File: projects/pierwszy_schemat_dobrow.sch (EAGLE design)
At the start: 30 parts, among them IC1 74HC595N, IC2 7805T, U1 ARDUINOR3-BPLACE

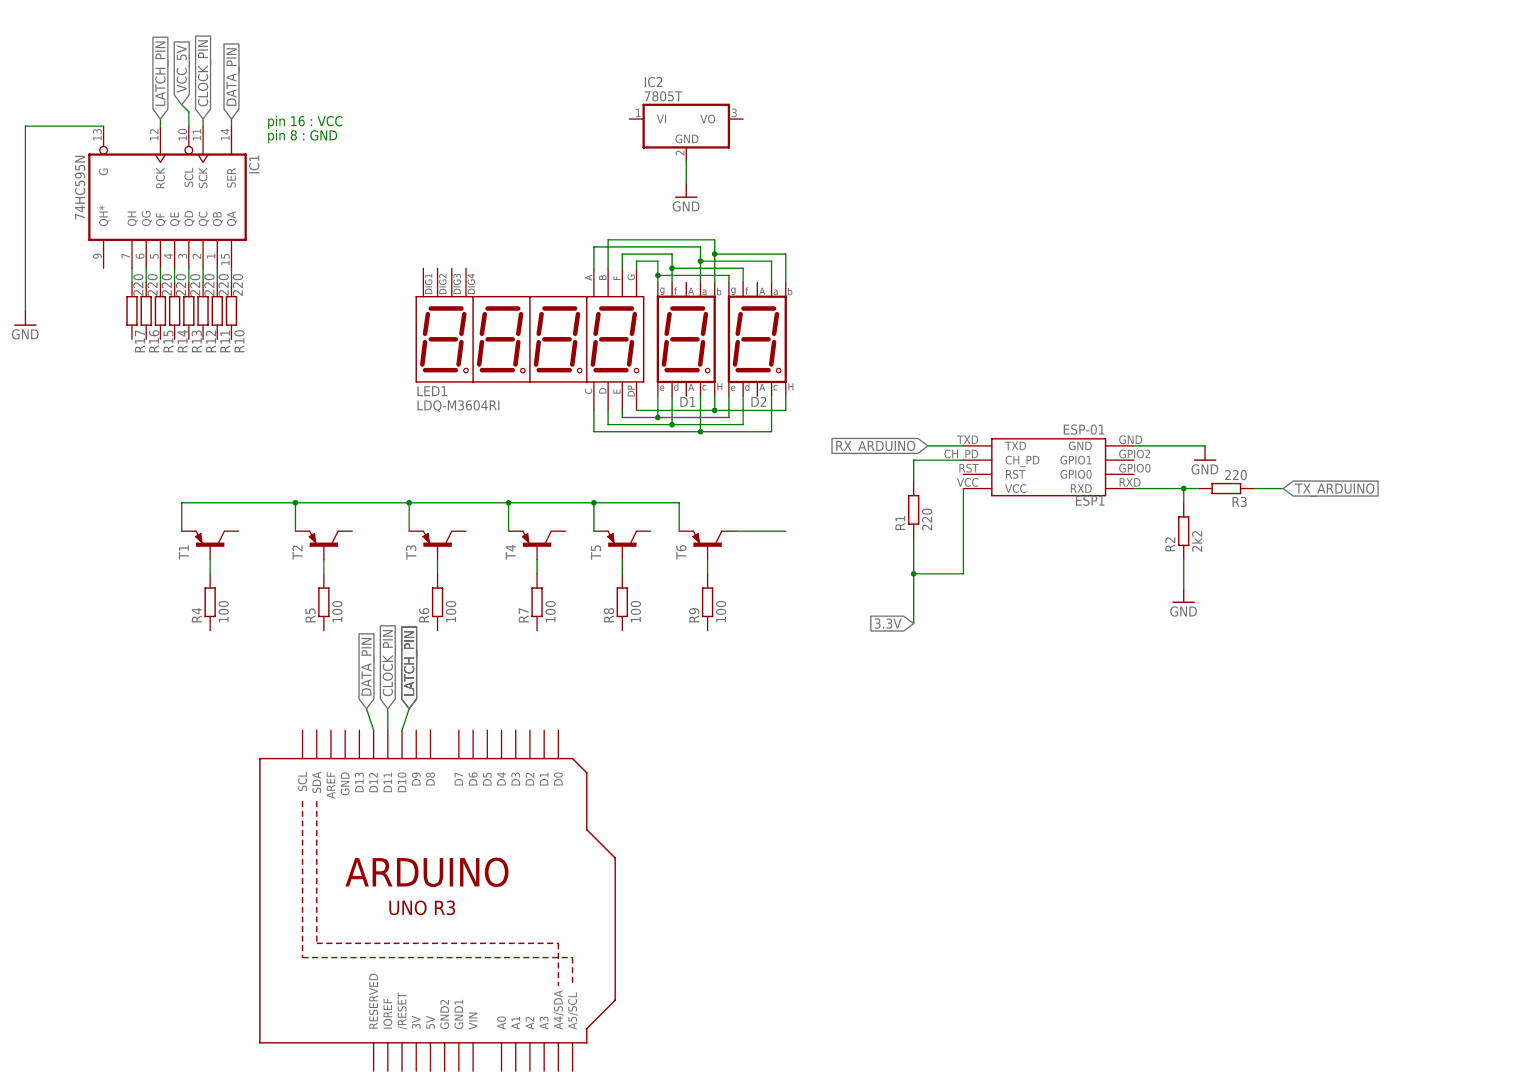
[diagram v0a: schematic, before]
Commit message: new arduino uno symbol
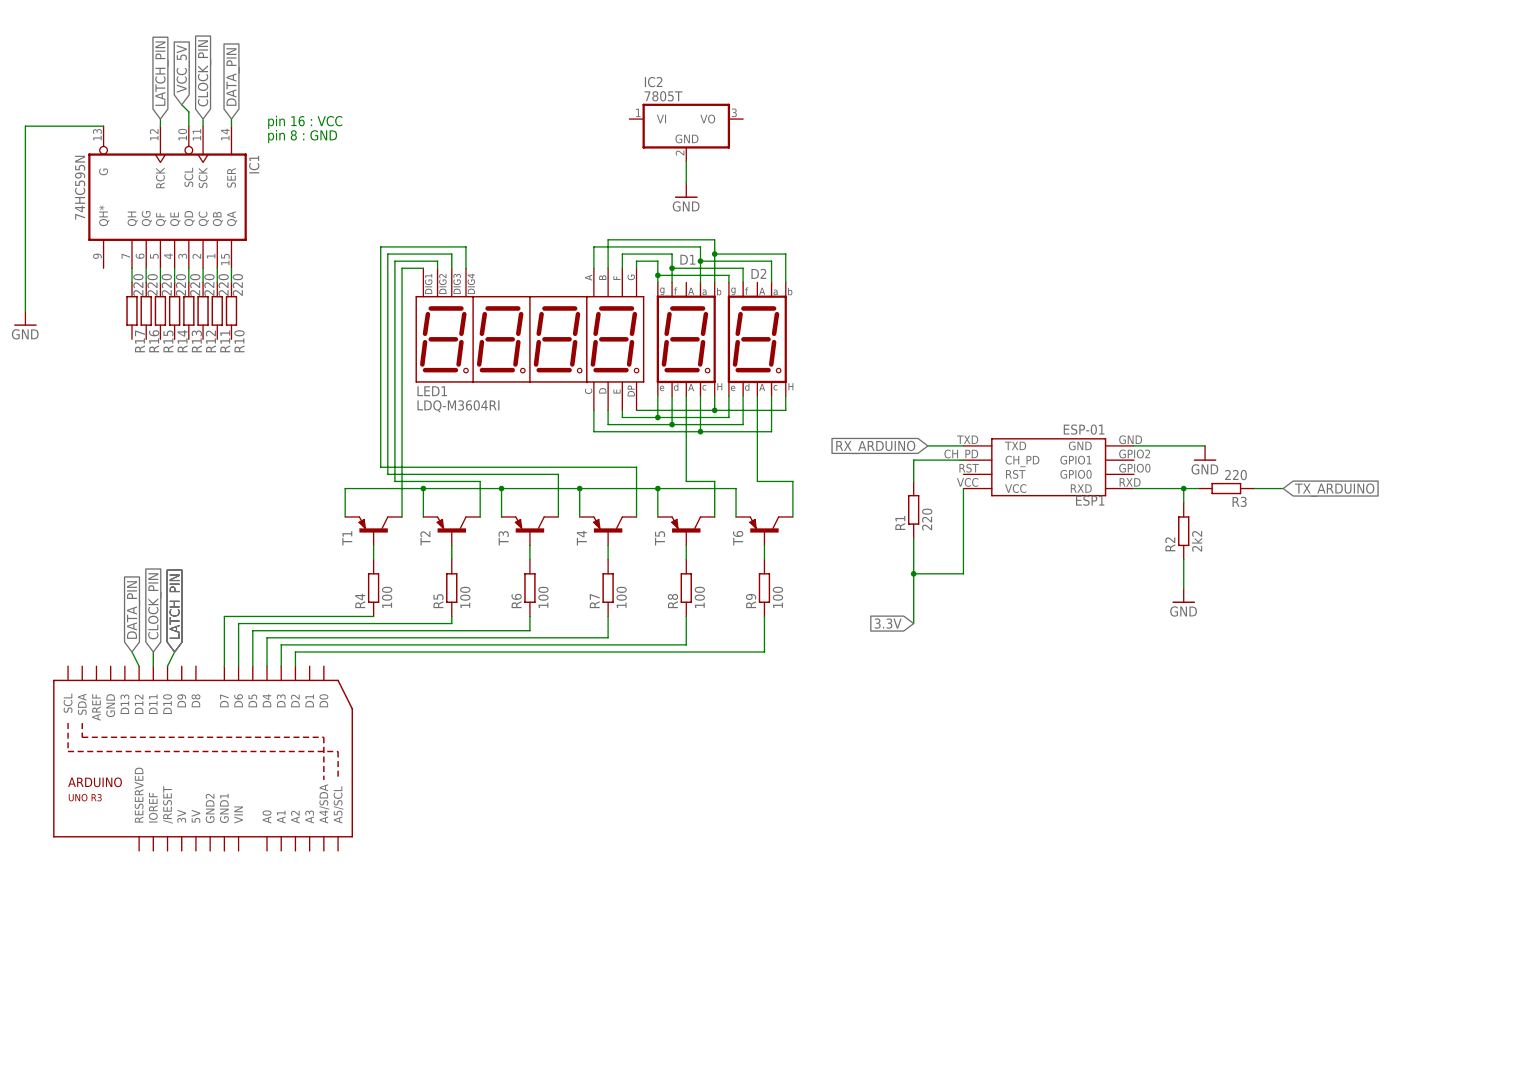
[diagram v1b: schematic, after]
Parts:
- removed U1: ARDUINOR3-BPLACE, adafruit:ARDUINOR3-BPLACE
- added U2: ARDUINOR3-DIMENSION, arduino_UNO_edit:ARDUINOR3-DIMENSION
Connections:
- new net N$26: LED1.DIG1, T1.C
- new net N$27: LED1.DIG3, T3.C
- new net N$28: LED1.DIG4, T4.C
- new net N$29: D1.CA2, T5.C
- new net N$30: D2.CA2, T6.C
- new net N$31: R4.1, U2.D7
- new net N$32: R5.1, U2.D6
- new net N$33: R6.1, U2.D5
- new net N$34: R7.1, U2.D4
- new net N$35: R8.1, U2.D3
- new net N$36: R9.1, U2.D2
- net CLOCK_PIN: now also U2.D11; no longer U1.D11
- net DATA_PIN: now also U2.D12; no longer U1.D12
- net LATCH_PIN: now also U2.D10; no longer U1.D10
- net N$8: now also LED1.DIG2, T2.C; no longer T6.C
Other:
- moved on the sheet: R4, R5, R6, R7, R8, R9, T1, T2, T3, T4, T5, T6

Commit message: added labels
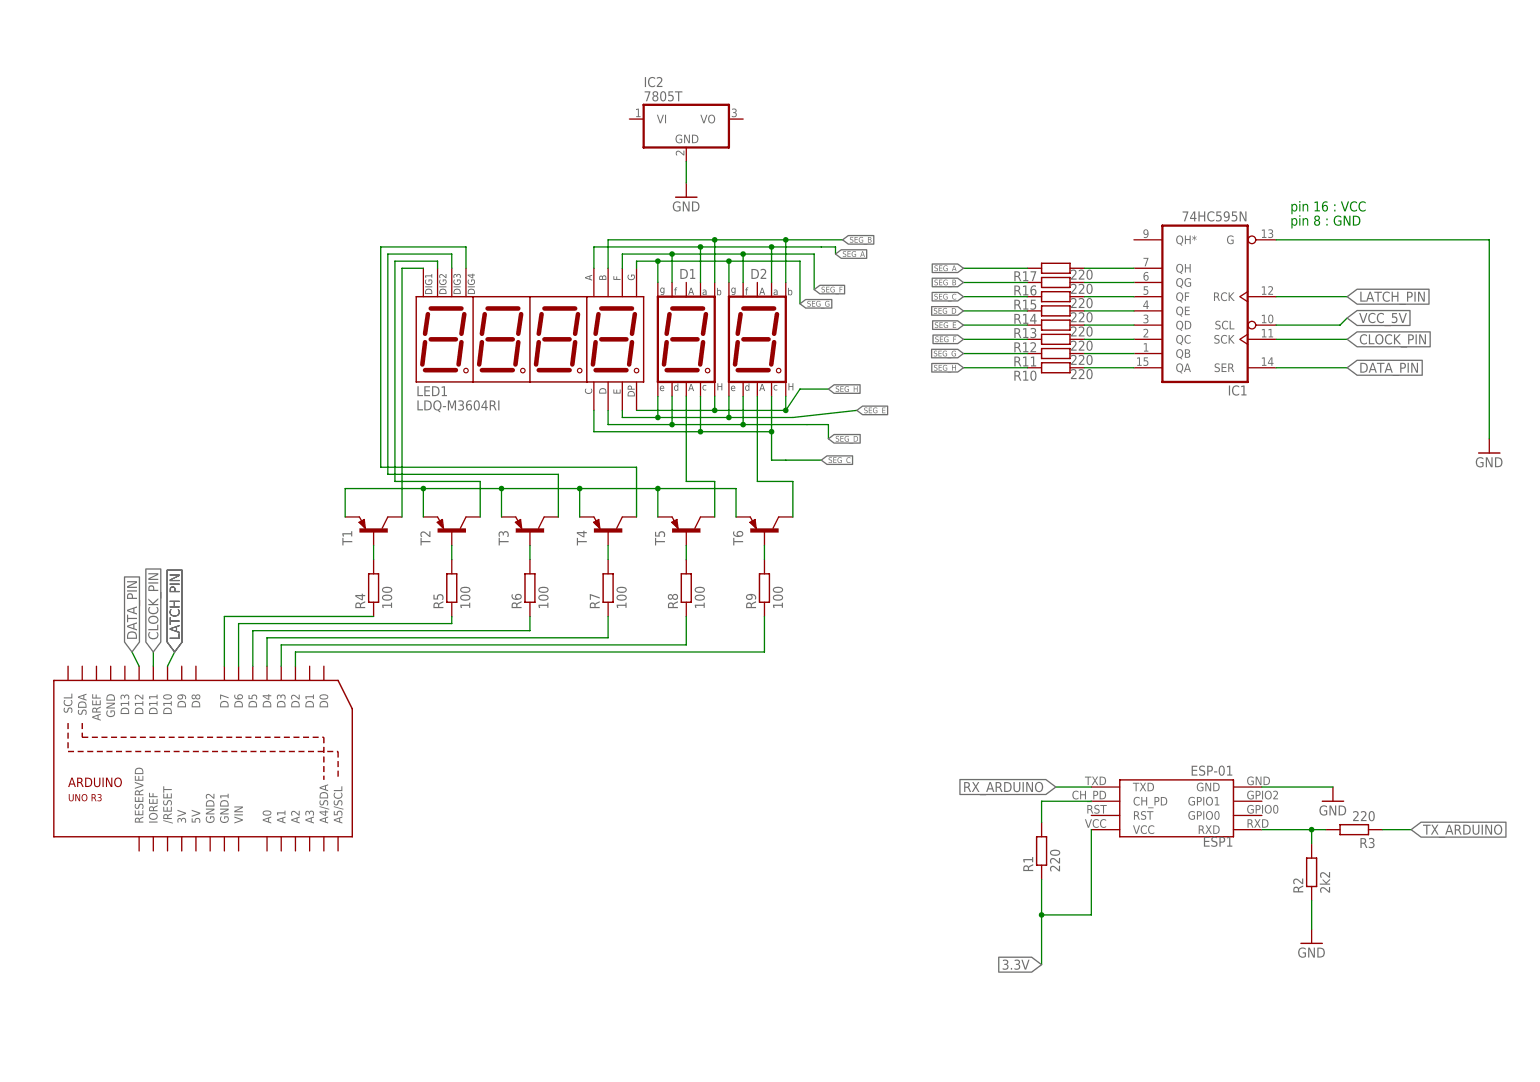
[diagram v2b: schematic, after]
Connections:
- removed net N$11: D1.F, D2.F, LED1.F
- removed net N$20: D1.DP, D2.DP, LED1.DP
- removed net N$21: D1.E, D2.E, LED1.E
- removed net N$22: D1.A, D2.A, LED1.A
- removed net N$23: D1.B, D2.B, LED1.B
- removed net N$24: D1.D, D2.D, LED1.D
- removed net N$25: D1.C, D2.C, LED1.C
- removed net N$9: D1.G, D2.G, LED1.G
- new net SEG_A: D1.A, D2.A, LED1.A, R17.1
- new net SEG_B: D1.B, D2.B, LED1.B, R16.1
- new net SEG_C: D1.C, D2.C, LED1.C, R15.1
- new net SEG_D: D1.D, D2.D, LED1.D, R14.1
- new net SEG_E: D1.E, D2.E, LED1.E, R13.1
- new net SEG_F: D1.F, D2.F, LED1.F, R12.1
- new net SEG_G: D1.G, D2.G, LED1.G, R11.1
- new net SEG_H: D1.DP, D2.DP, LED1.DP, R10.1
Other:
- moved on the sheet: ESP1, IC1, R1, R10, R11, R12, R13, R14, R15, R16, R17, R2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
